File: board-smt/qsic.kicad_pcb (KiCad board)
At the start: 2 copper layers, 217.7 x 134 mm, 86 parts, among them Q201 Dual_NMOS, Q202 Dual_NMOS, Q203 Dual_NMOS, Q204 Dual_NMOS, Q205 Dual_NMOS, Q206 Dual_NMOS, Q209 Dual_NMOS, Q210 Dual_NMOS, Q211 Dual_NMOS, Q213 Dual_NMOS, Q214 Dual_NMOS, Q215 Dual_NMOS, Q218 Dual_NMOS, Q219 Dual_NMOS, Q220 Dual_NMOS, Q222 Dual_NMOS, Q223 Dual_NMOS, Q224 Dual_NMOS, Q228 Dual_NMOS, Q229 Dual_NMOS, Q232 Dual_NMOS, Q233 Dual_NMOS, Q235 Dual_NMOS, Q236 Dual_NMOS, Q239 Dual_NMOS, Q240 Dual_NMOS, Q244 Dual_NMOS, Q245 Dual_NMOS, Q247 Dual_NMOS, Q248 Dual_NMOS, Q251 Dual_NMOS, Q252 Dual_NMOS, Q254 Dual_NMOS, Q255 Dual_NMOS, Q256 Dual_NMOS, Q257 Dual_NMOS, Q258 Dual_NMOS, Q259 Dual_NMOS, Q261 Dual_NMOS

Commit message: Added board-prototype.
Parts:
- added REF**: BGA-256_pitch1mm_dia0.4mm, SMD_Packages:BGA-256_pitch1mm_dia0.4mm, F.Cu at (112.0, 72.2)
- added REF**: 10-SRT, myMods.pretty:10-SRT, F.Cu at (199.9, 48.1)
- added REF**: SOIC-16_3.9x9.9mm_Pitch1.27mm, Housings_SOIC:SOIC-16_3.9x9.9mm_Pitch1.27mm, F.Cu at (163.2, 39.2)
- moved R243 30.6 mm to (213.1, 70.1), turned to 270 degrees
- moved R245 25.3 mm to (209.2, 69.1), turned to 180 degrees
- moved R246 23.6 mm to (209.2, 76.1), turned to 180 degrees
- moved R239 21.6 mm to (213.1, 57.5), turned to 270 degrees
- moved R240 21.2 mm to (213.1, 61.0), turned to 90 degrees
- moved R241 17.7 mm to (210.8, 57.5), turned to 90 degrees
- moved R244 17.7 mm to (213.1, 73.5), turned to 90 degrees
- moved R242 16.7 mm to (210.8, 61.0), turned to 270 degrees
- moved Q256 15.5 mm to (207.3, 59.4)
- moved Q258 13.6 mm to (209.2, 72.4)
- moved R237 8.90 mm to (202.4, 72.4)
- moved R235 8.89 mm to (202.4, 59.4)
- moved R223 6.48 mm to (217.7, 62.5)
- moved R201 6.36 mm to (217.7, 65.7)
- moved R202 6.35 mm to (217.7, 78.4)
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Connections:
- B101 pad AB2: -12V -> Net-(B101-PadAB2)
- B101 pad AD2: +12V -> Net-(B101-PadAD2)
- B101 pad BB2: -12V -> Net-(B101-PadBB2)
- B101 pad BD2: +12V -> Net-(B101-PadBD2)
- Q256 pad 3: RIRQ6 -> RIAKI
- Q258 pad 3: RIRQ7 -> RDMGI
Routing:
- net (no net): track 0.00 -> 158.7 mm, vias 0 -> 12
- net +5V: track 0.00 -> 71.5 mm, vias 0 -> 4
- net GND: track 334.7 -> 372.6 mm, vias 0 -> 2
- net BDMGI: track 16.8 -> 39.5 mm
- net BDMGO: track 15.1 -> 31.5 mm
- net BIAKI: track 15.0 -> 31.1 mm
- net BIAKO: track 16.8 -> 32.6 mm
- net BBS7: track 22.5 -> 16.0 mm
- net BWTBT: track 21.8 -> 15.9 mm
- net BSYNC: track 21.8 -> 15.9 mm
- net BRPLY: track 21.8 -> 15.9 mm
- net BIRQ4: track 21.8 -> 15.9 mm
- net BINIT: track 21.8 -> 15.9 mm
- net BDOUT: track 21.8 -> 15.9 mm
- net BDIN: track 21.8 -> 15.9 mm
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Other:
- net class Default: clearance 0.254 -> 0.2032
- net class s5 added: clearance 0.127, trace_width 0.127, via_dia 0.3048, via_drill 0.254
- rule trace_clearance: 0.254 -> 0.2032

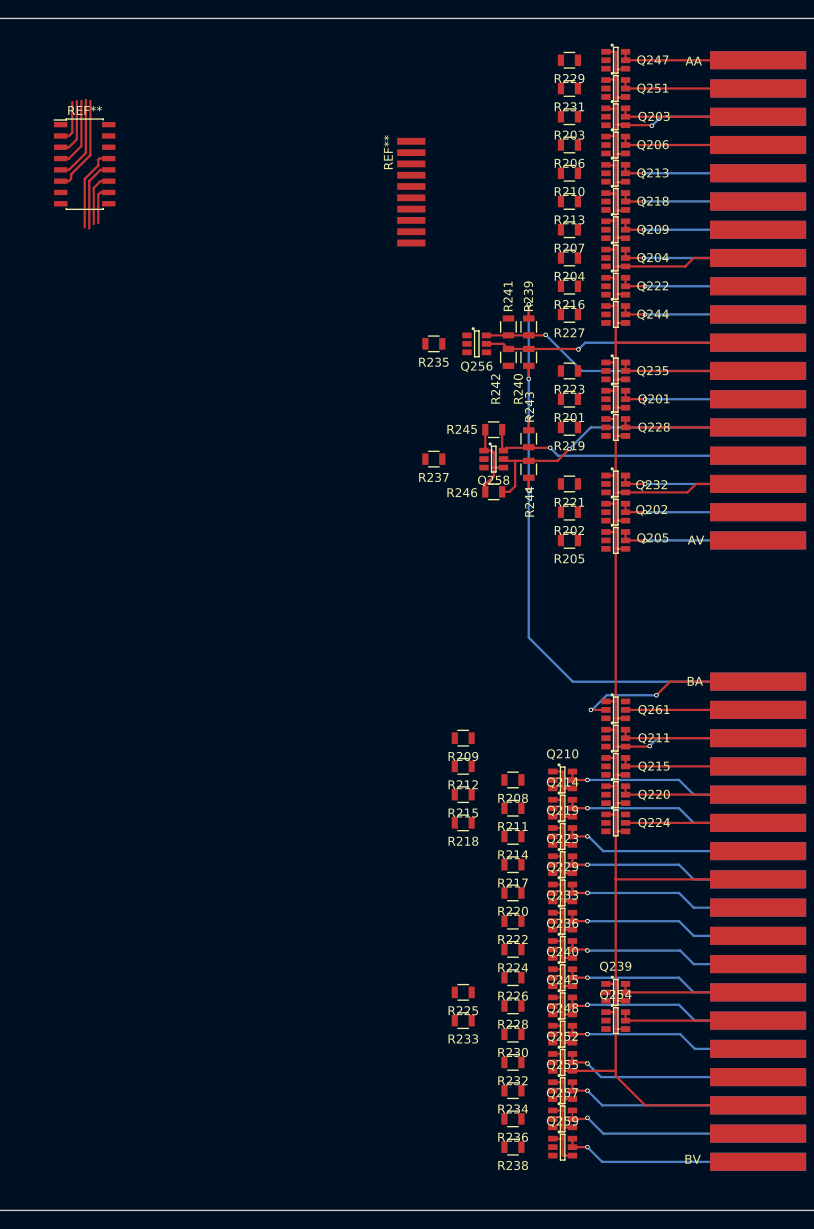
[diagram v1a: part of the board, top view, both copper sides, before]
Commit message: Added bus termination.
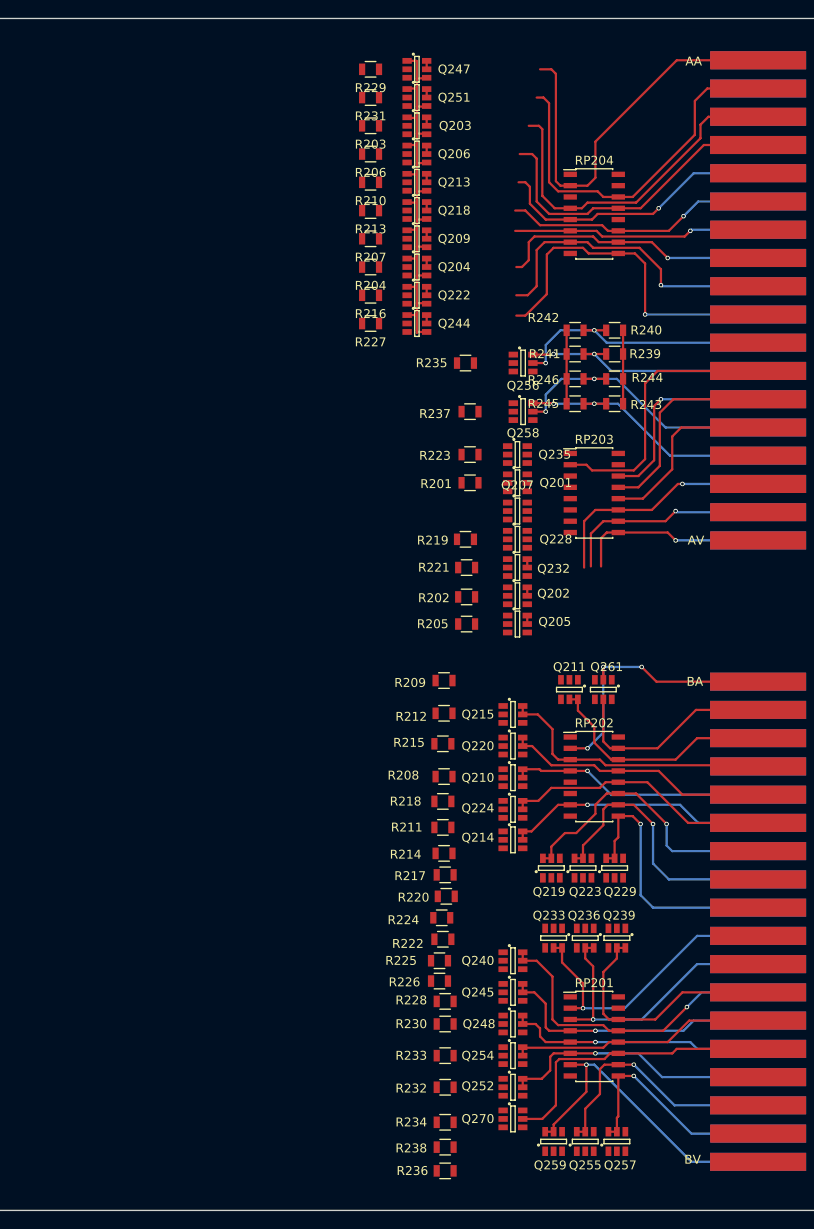
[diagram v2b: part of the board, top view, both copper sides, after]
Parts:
- removed the REF** at (199.9, 48.1)
- removed the REF** at (163.2, 39.2)
- added Q207: Dual_NMOS, TO_SOT_Packages_SMD:SOT-23-6, F.Cu at (211.8, 78.2)
- added Q270: Dual_NMOS, TO_SOT_Packages_SMD:SOT-23-6, F.Cu at (211.3, 146.6)
- added RP201: 330,680, Housings_SOIC:SOIC-16_3.9x9.9mm_Pitch1.27mm, F.Cu at (220.5, 137.3)
- added RP202: 330,680, Housings_SOIC:SOIC-16_3.9x9.9mm_Pitch1.27mm, F.Cu at (220.5, 108.1)
- added RP203: 330,680, Housings_SOIC:SOIC-16_3.9x9.9mm_Pitch1.27mm, F.Cu at (220.5, 76.2)
- added RP204: 330,680, Housings_SOIC:SOIC-16_3.9x9.9mm_Pitch1.27mm, F.Cu at (220.5, 44.8)
- B201: renamed from B101; value QBus -> QBUS
- R239, R240, R243, R244: value R -> 390
- R241, R242, R245, R246: value R -> 680
- moved Q203 22.4 mm to (200.5, 34.9)
- moved Q204 22.4 mm to (200.5, 50.8)
- moved Q206 22.4 mm to (200.5, 38.1)
- moved Q209 22.4 mm to (200.5, 47.6)
- moved Q213 22.4 mm to (200.5, 41.3)
- moved Q218 22.4 mm to (200.5, 44.5)
- moved Q222 22.4 mm to (200.5, 54.0)
- moved Q244 22.4 mm to (200.5, 57.1)
- moved Q247 22.4 mm to (200.5, 28.6)
- moved Q251 22.4 mm to (200.5, 31.8)
- moved R203 22.4 mm to (195.3, 34.9)
- moved R204 22.4 mm to (195.3, 50.8)
- moved R206 22.4 mm to (195.3, 38.1)
- moved R207 22.4 mm to (195.3, 47.6)
- moved R210 22.4 mm to (195.3, 41.3)
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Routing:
- net GND: track 372.6 -> 62.2 mm, vias 2 -> 0
- net (no net): track 158.7 -> 90.7 mm
- net +5V: track 71.5 -> 8.26 mm, vias 4 -> 0
- net BEVNT: track 0.00 -> 32.7 mm
- net BIRQ5: track 15.9 -> 46.2 mm
- net BIRQ6: track 15.9 -> 43.0 mm
- net BIRQ4: track 15.9 -> 40.3 mm
- net BDAL16: track 15.9 -> 40.1 mm
- net BHALT: track 0.00 -> 23.3 mm
- net BDAL17: track 15.9 -> 36.6 mm
- net BWTBT: track 15.9 -> 36.1 mm
- net BDOUT: track 15.9 -> 32.9 mm
- net BSYNC: track 15.9 -> 31.7 mm
- net BDAL19: track 16.0 -> 31.5 mm
- net BDAL21: track 15.0 -> 30.2 mm
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
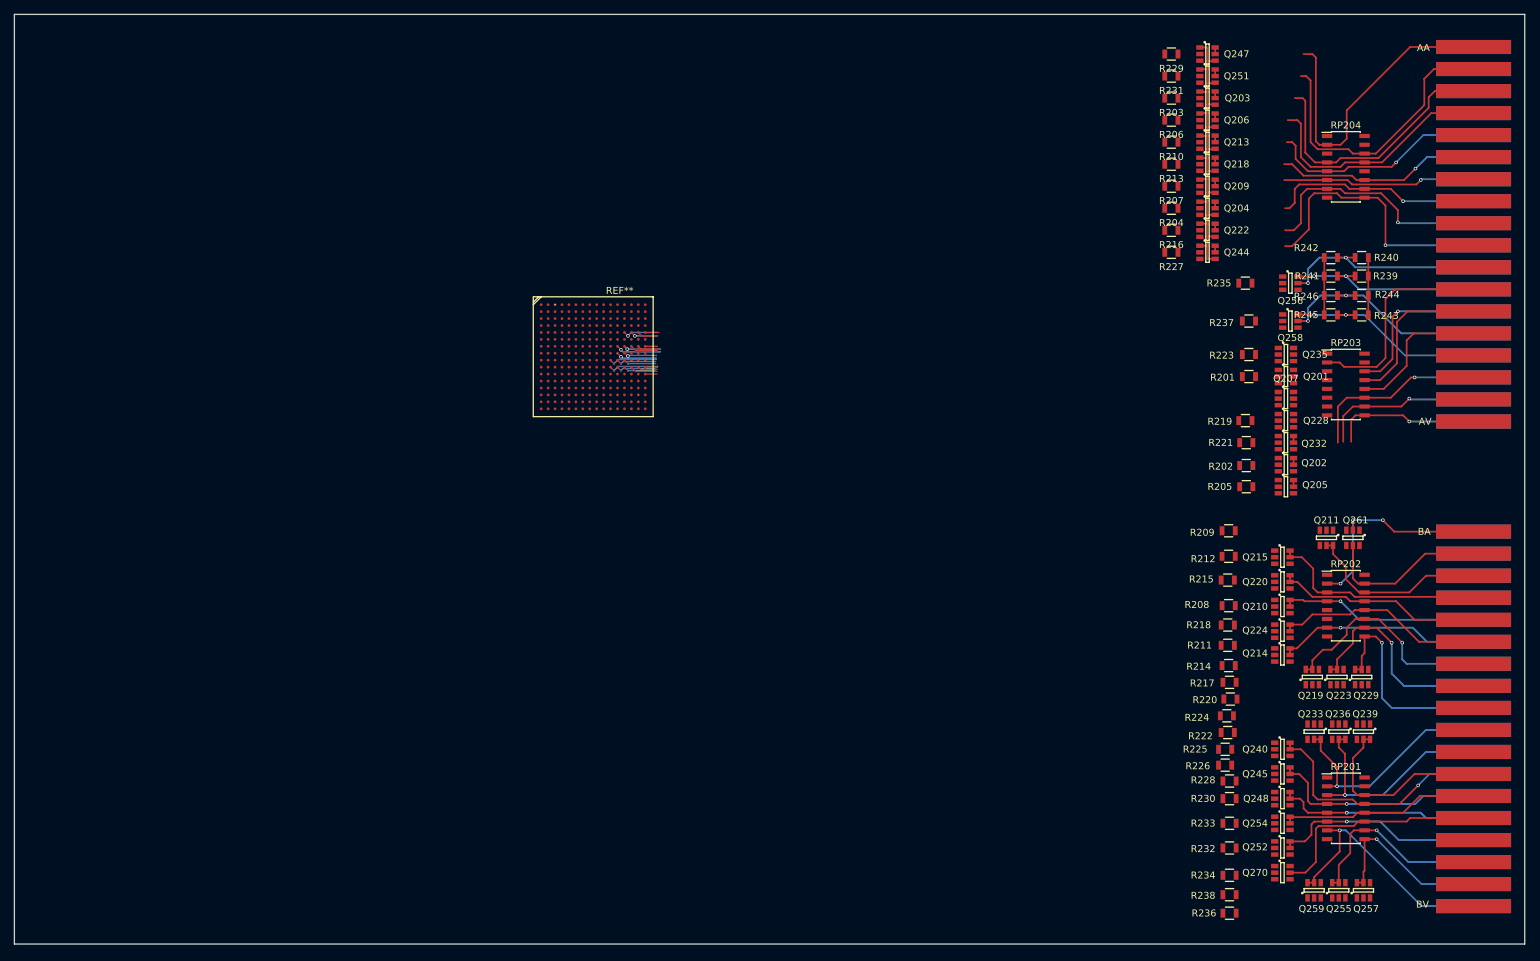
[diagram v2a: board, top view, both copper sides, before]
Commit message: Changed to comparator for bus receivers and rearranged schematic to multiple pages
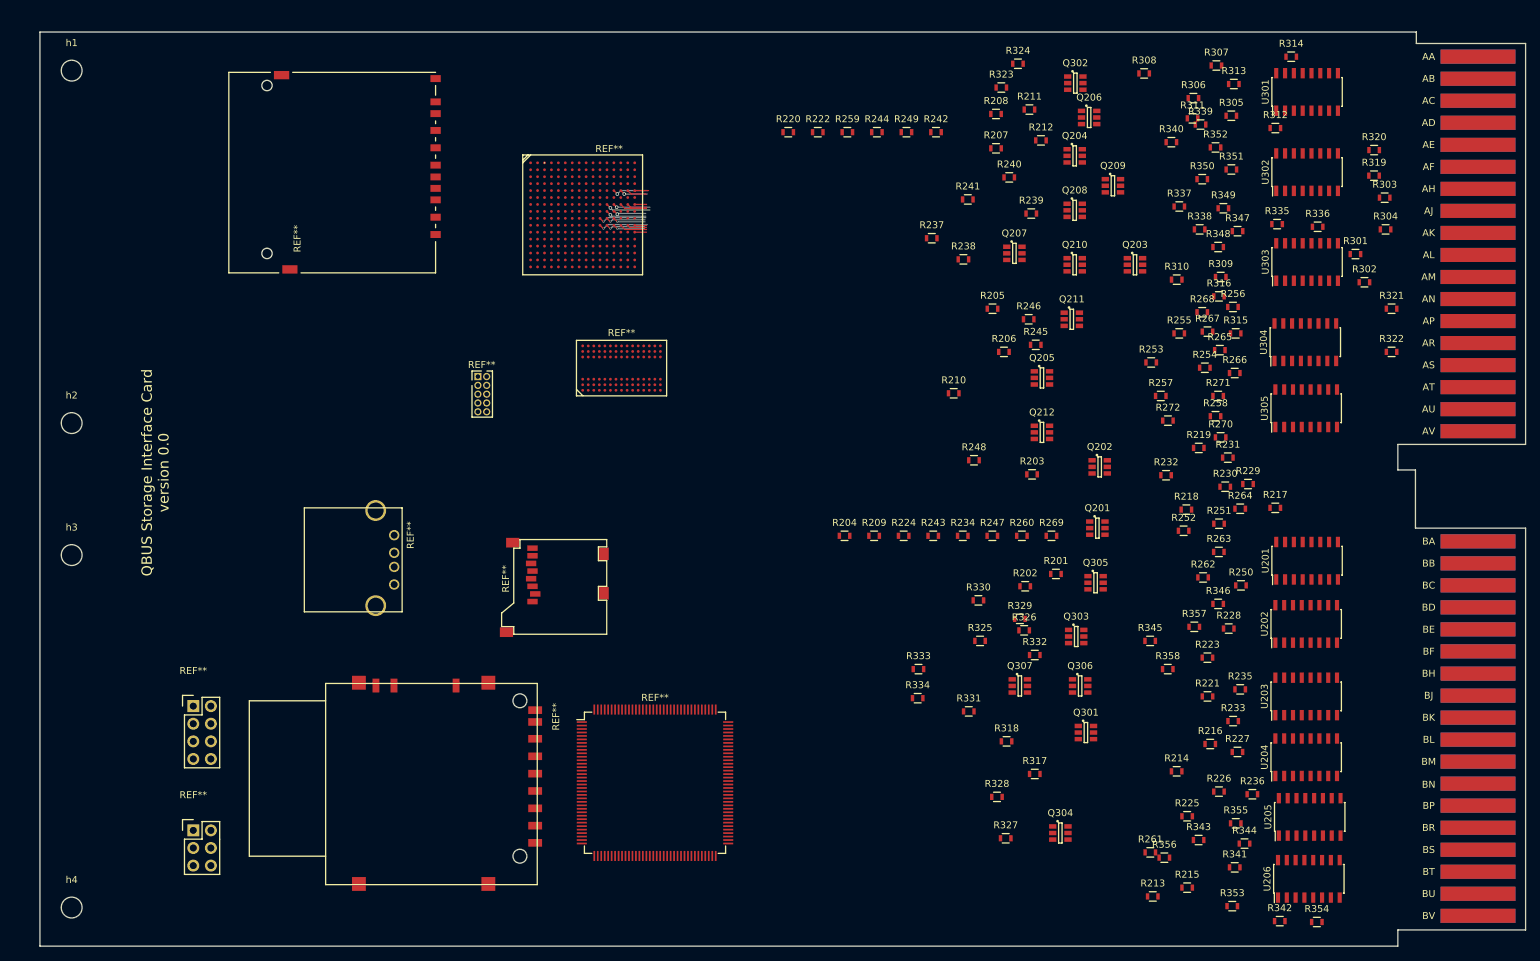
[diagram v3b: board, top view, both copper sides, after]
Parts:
- removed B201: QBUS, myMods.pretty:Qbus-double
- removed Q213, Q214, Q215, Q218, Q219, Q220, Q222, Q223, Q224, Q228, Q229, Q232, Q233, Q235, Q236, Q239, Q240, Q244, Q245, Q247, Q248, Q251, Q252, Q254, Q255, Q256, Q257, Q258, Q259, Q261, Q270: Dual_NMOS, TO_SOT_Packages_SMD:SOT-23-6
- removed RP201, RP202, RP203, RP204: 330,680, Housings_SOIC:SOIC-16_3.9x9.9mm_Pitch1.27mm
- added B101: QBUS, myMods.pretty:Qbus-double, F.Cu at (246.4, 25.4)
- added Q208: Dual_NMOS, TO_SOT_Packages_SMD:SOT-23-6, F.Cu at (181.4, 51.1)
- added Q212: Dual_NMOS, TO_SOT_Packages_SMD:SOT-23-6, F.Cu at (176.7, 83.1)
- added Q301: Dual_NMOS, TO_SOT_Packages_SMD:SOT-23-6, F.Cu at (183.0, 126.4)
- added Q302: Dual_NMOS, TO_SOT_Packages_SMD:SOT-23-6, F.Cu at (181.5, 32.8)
- added Q303: Dual_NMOS, TO_SOT_Packages_SMD:SOT-23-6, F.Cu at (181.6, 112.5)
- added Q304: Dual_NMOS, TO_SOT_Packages_SMD:SOT-23-6, F.Cu at (179.3, 140.8)
- added Q305: Dual_NMOS, TO_SOT_Packages_SMD:SOT-23-6, F.Cu at (184.4, 104.8)
- added Q306: Dual_NMOS, TO_SOT_Packages_SMD:SOT-23-6, F.Cu at (182.2, 119.6)
- added Q307: Dual_NMOS, TO_SOT_Packages_SMD:SOT-23-6, F.Cu at (173.5, 119.6)
- added R247: R, Resistors_SMD:R_0603, F.Cu at (169.5, 98.0)
- added R248: R, Resistors_SMD:R_0603, F.Cu at (166.9, 87.1)
- added R249: R, Resistors_SMD:R_0603, F.Cu at (157.1, 39.8)
- added R250: R, Resistors_SMD:R_0603, F.Cu at (205.4, 105.2)
- added R251: R, Resistors_SMD:R_0603, F.Cu at (202.2, 96.3)
- added R252: R, Resistors_SMD:R_0603, F.Cu at (197.1, 97.3)
- added R253: R, Resistors_SMD:R_0603, F.Cu at (192.4, 73.0)
- added R254: R, Resistors_SMD:R_0603, F.Cu at (200.2, 73.8)
- added R255: R, Resistors_SMD:R_0603, F.Cu at (196.5, 68.8)
- added R256: R, Resistors_SMD:R_0603, F.Cu at (204.2, 65.0)
- added R257: R, Resistors_SMD:R_0603, F.Cu at (193.8, 77.9)
- added R258: R, Resistors_SMD:R_0603, F.Cu at (201.7, 80.8)
- added R259: R, Resistors_SMD:R_0603, F.Cu at (148.6, 39.8)
- added R260: R, Resistors_SMD:R_0603, F.Cu at (173.8, 98.0)
- added R261: R, Resistors_SMD:R_0603, F.Cu at (192.3, 143.6)
- added R262: R, Resistors_SMD:R_0603, F.Cu at (199.9, 104.0)
- added R263: R, Resistors_SMD:R_0603, F.Cu at (202.2, 100.3)
- added R264: R, Resistors_SMD:R_0603, F.Cu at (205.2, 94.1)
- added R265: R, Resistors_SMD:R_0603, F.Cu at (202.3, 71.2)
- added R266: R, Resistors_SMD:R_0603, F.Cu at (204.5, 74.5)
- added R267: R, Resistors_SMD:R_0603, F.Cu at (200.5, 68.6)
- added R268: R, Resistors_SMD:R_0603, F.Cu at (199.8, 65.8)
- added R269: R, Resistors_SMD:R_0603, F.Cu at (178.0, 98.0)
- added R270: R, Resistors_SMD:R_0603, F.Cu at (202.4, 83.8)
- added R271: R, Resistors_SMD:R_0603, F.Cu at (202.1, 77.9)
- added R272: R, Resistors_SMD:R_0603, F.Cu at (194.8, 81.4)
- added R301: 330, Resistors_SMD:R_0603, F.Cu at (221.9, 57.4)
- added R302: 680, Resistors_SMD:R_0603, F.Cu at (223.2, 61.5)
- added R303: 330, Resistors_SMD:R_0603, F.Cu at (226.1, 49.3)
- added R304: 680, Resistors_SMD:R_0603, F.Cu at (226.2, 53.8)
- added R305: R, Resistors_SMD:R_0603, F.Cu at (204.0, 37.5)
- added R306: R, Resistors_SMD:R_0603, F.Cu at (198.5, 34.9)
- added R307: R, Resistors_SMD:R_0603, F.Cu at (201.8, 30.2)
- added R308: R, Resistors_SMD:R_0603, F.Cu at (191.4, 31.4)
- added R309: R, Resistors_SMD:R_0603, F.Cu at (202.4, 60.7)
- added R310: R, Resistors_SMD:R_0603, F.Cu at (196.1, 61.1)
- added R311: R, Resistors_SMD:R_0603, F.Cu at (198.4, 37.8)
- added R312: R, Resistors_SMD:R_0603, F.Cu at (210.3, 39.2)
- added R313: R, Resistors_SMD:R_0603, F.Cu at (204.3, 32.9)
- added R314: R, Resistors_SMD:R_0603, F.Cu at (212.6, 29.0)
- added R315: R, Resistors_SMD:R_0603, F.Cu at (204.6, 68.8)
- added R316: R, Resistors_SMD:R_0603, F.Cu at (202.2, 63.5)
- added R317: R, Resistors_SMD:R_0603, F.Cu at (175.6, 132.3)
- added R318: R, Resistors_SMD:R_0603, F.Cu at (171.6, 127.6)
- added R319: 330, Resistors_SMD:R_0603, F.Cu at (224.5, 46.1)
- added R320: 680, Resistors_SMD:R_0603, F.Cu at (224.5, 42.4)
- added R321: 330, Resistors_SMD:R_0603, F.Cu at (227.1, 65.3)
- added R322: 680, Resistors_SMD:R_0603, F.Cu at (227.1, 71.5)
- added R323: R, Resistors_SMD:R_0603, F.Cu at (170.8, 33.4)
- added R324: R, Resistors_SMD:R_0603, F.Cu at (173.2, 30.0)
- added R325: R, Resistors_SMD:R_0603, F.Cu at (167.8, 113.2)
- added R326: R, Resistors_SMD:R_0603, F.Cu at (174.1, 111.6)
- added R327: R, Resistors_SMD:R_0603, F.Cu at (171.4, 141.6)
- added R328: R, Resistors_SMD:R_0603, F.Cu at (170.2, 135.6)
- added R329: R, Resistors_SMD:R_0603, F.Cu at (173.5, 110.0)
- added R330: R, Resistors_SMD:R_0603, F.Cu at (167.5, 107.3)
- added R331: R, Resistors_SMD:R_0603, F.Cu at (166.1, 123.3)
- added R332: R, Resistors_SMD:R_0603, F.Cu at (175.6, 115.2)
- added R333: R, Resistors_SMD:R_0603, F.Cu at (158.9, 117.2)
- added R334: R, Resistors_SMD:R_0603, F.Cu at (158.8, 121.4)
- added R335: R, Resistors_SMD:R_0603, F.Cu at (210.6, 53.1)
- added R336: R, Resistors_SMD:R_0603, F.Cu at (216.4, 53.5)
- added R337: R, Resistors_SMD:R_0603, F.Cu at (196.5, 50.5)
- added R338: R, Resistors_SMD:R_0603, F.Cu at (199.4, 53.8)
- added R339: R, Resistors_SMD:R_0603, F.Cu at (199.5, 38.7)
- added R340: R, Resistors_SMD:R_0603, F.Cu at (195.3, 41.3)
- added R341: R, Resistors_SMD:R_0603, F.Cu at (204.5, 145.8)
- added R342: R, Resistors_SMD:R_0603, F.Cu at (210.9, 153.5)
- added R343: R, Resistors_SMD:R_0603, F.Cu at (199.3, 141.9)
- added R344: R, Resistors_SMD:R_0603, F.Cu at (205.9, 142.4)
- added R345: R, Resistors_SMD:R_0603, F.Cu at (192.3, 113.2)
- added R346: R, Resistors_SMD:R_0603, F.Cu at (202.1, 107.8)
- added R347: R, Resistors_SMD:R_0603, F.Cu at (204.9, 54.1)
- added R348: R, Resistors_SMD:R_0603, F.Cu at (202.1, 56.4)
- added R349: R, Resistors_SMD:R_0603, F.Cu at (202.8, 50.8)
- added R350: R, Resistors_SMD:R_0603, F.Cu at (199.8, 46.6)
- added R351: R, Resistors_SMD:R_0603, F.Cu at (204.0, 45.2)
- added R352: R, Resistors_SMD:R_0603, F.Cu at (201.7, 42.0)
- added R353: R, Resistors_SMD:R_0603, F.Cu at (204.1, 151.4)
- added R354: R, Resistors_SMD:R_0603, F.Cu at (216.3, 153.7)
- added R355: R, Resistors_SMD:R_0603, F.Cu at (204.6, 139.4)
- added R356: R, Resistors_SMD:R_0603, F.Cu at (194.3, 144.4)
- added R357: R, Resistors_SMD:R_0603, F.Cu at (198.6, 111.1)
- added R358: R, Resistors_SMD:R_0603, F.Cu at (194.8, 117.2)
- added REF**: microSD 3M, myMods.pretty:microSD-3M-2900-series, F.Cu at (101.3, 98.3)
- added REF**: DEC Handle, myMods.pretty:DEC-Handle, F.Cu at (32.3, 126.1)
- added REF**: DEC Handle, myMods.pretty:DEC-Handle, F.Cu at (32.3, 56.4)
- added REF**: BGA-90-0.8mm, SMD_Packages:BGA-90-0.8mm, F.Cu at (116.1, 73.8)
- added REF**: TQFP-144_20x20mm_Pitch0.5mm, Housings_QFP:TQFP-144_20x20mm_Pitch0.5mm, F.Cu at (120.9, 133.6)
- added REF**: USB_A, Connect:USB_A, F.Cu at (83.3, 97.9)
- added REF**: SD_Card_Receptacle, Connect:SD_Card_Receptacle, F.Cu at (89.3, 45.2)
- added REF**: Pin_Header_Straight_2x04, Pin_Headers:Pin_Header_Straight_2x04, F.Cu at (54.4, 122.6)
- added REF**: Pin_Header_Straight_2x03, Pin_Headers:Pin_Header_Straight_2x03, F.Cu at (54.4, 140.5)
- added REF**: Pin_Header_Straight_2x05_Pitch1.27mm, Pin_Headers:Pin_Header_Straight_2x05_Pitch1.27mm, F.Cu at (95.4, 75.1)
- added REF**: SD Card DM1, myMods.pretty:SD-Card-DM1, F.Cu at (101.4, 121.8)
- added U201: CMP401, Housings_SOIC:SOIC-16_3.9x9.9mm_Pitch1.27mm, F.Cu at (214.9, 101.6)
- added U202: CMP401, Housings_SOIC:SOIC-16_3.9x9.9mm_Pitch1.27mm, F.Cu at (214.8, 110.7)
- added U203: CMP401, Housings_SOIC:SOIC-16_3.9x9.9mm_Pitch1.27mm, F.Cu at (214.8, 121.2)
- added U204: CMP401, Housings_SOIC:SOIC-16_3.9x9.9mm_Pitch1.27mm, F.Cu at (214.8, 129.9)
- added U205: CMP401, Housings_SOIC:SOIC-16_3.9x9.9mm_Pitch1.27mm, F.Cu at (215.3, 138.5)
- added U206: CMP401, Housings_SOIC:SOIC-16_3.9x9.9mm_Pitch1.27mm, F.Cu at (215.1, 147.4)
- added U301: CMP401, Housings_SOIC:SOIC-16_3.9x9.9mm_Pitch1.27mm, F.Cu at (214.9, 34.0)
- added U302: CMP401, Housings_SOIC:SOIC-16_3.9x9.9mm_Pitch1.27mm, F.Cu at (214.9, 45.6)
- added U303: CMP401, Housings_SOIC:SOIC-16_3.9x9.9mm_Pitch1.27mm, F.Cu at (214.9, 58.5)
- added U304: CMP401, Housings_SOIC:SOIC-16_3.9x9.9mm_Pitch1.27mm, F.Cu at (214.6, 70.1)
- added U305: CMP401, Housings_SOIC:SOIC-16_3.9x9.9mm_Pitch1.27mm, F.Cu at (214.8, 79.6)
- added h1: MountingHole_3mm, Mounting_Holes:MountingHole_3mm, F.Cu at (36.8, 31.0)
- added h2: MountingHole_3mm, Mounting_Holes:MountingHole_3mm, F.Cu at (36.8, 81.8)
- added h3: MountingHole_3mm, Mounting_Holes:MountingHole_3mm, F.Cu at (36.8, 100.8)
- added h4: MountingHole_3mm, Mounting_Holes:MountingHole_3mm, F.Cu at (36.8, 151.6)
- R201, R202, R203, R204, R205, R206, R207, R208, R209, R210, R211, R212, R213, R214, R215, R216, R217, R218, R219, R220, R221, R222, R223, R224, R225, R226, R227, R228, R229, R230, R231, R232, R233, R234, R235, R236, R237, R238: footprint Resistors_SMD:R_0805 -> Resistors_SMD:R_0603
- R239, R240, R243, R244: value 390 -> R; footprint Resistors_SMD:R_0805 -> Resistors_SMD:R_0603
- R241, R242, R245, R246: value 680 -> R; footprint Resistors_SMD:R_0805 -> Resistors_SMD:R_0603
- moved R213 105.6 mm to (192.6, 150.0), turned to 0 degrees
- moved R222 104.8 mm to (144.4, 39.8), turned to 0 degrees
- moved R220 103.6 mm to (140.1, 39.8), turned to 0 degrees
- moved R238 99.3 mm to (165.4, 58.2), turned to 0 degrees
- moved R211 82.3 mm to (174.9, 36.6), turned to 0 degrees
- moved R208 78.4 mm to (170.1, 37.2), turned to 0 degrees
- moved R216 74.3 mm to (200.9, 128.0), turned to 0 degrees
- moved R244 73.7 mm to (152.9, 39.8), turned to 0 degrees
- moved R227 72.6 mm to (204.9, 129.2), turned to 0 degrees
- moved R243 69.5 mm to (161.0, 98.0), turned to 0 degrees
- moved R204 66.7 mm to (148.2, 98.0), turned to 0 degrees
- moved R212 65.8 mm to (176.5, 41.0), turned to 0 degrees
- moved R229 63.0 mm to (206.4, 90.6), turned to 0 degrees
- moved R234 62.2 mm to (165.3, 98.0), turned to 0 degrees
- moved R242 59.7 mm to (161.4, 39.8), turned to 0 degrees
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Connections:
- Q201 pad 3: RBS7 -> BDAL1
- Q201 pad 5: BBS7 -> Net-(Q201-Pad5)
- Q201 pad 6: BBS7 -> BDAL0
- Q202 pad 3: RDAL0 -> BDAL3
- Q202 pad 5: BDAL0 -> Net-(Q202-Pad5)
- Q202 pad 6: BDAL0 -> BDAL2
- Q203 pad 3: RDAL16 -> BDAL5
- Q203 pad 5: BDAL16 -> Net-(Q203-Pad5)
- Q203 pad 6: BDAL16 -> BDAL4
- Q204 pad 3: RSYNC -> BDAL7
- Q204 pad 5: BSYNC -> Net-(Q204-Pad5)
- Q204 pad 6: BSYNC -> BDAL6
- Q205 pad 3: RDAL1 -> BDAL9
- Q205 pad 5: BDAL1 -> Net-(Q205-Pad5)
- Q205 pad 6: BDAL1 -> BDAL8
- Q206 pad 3: RDAL17 -> BDAL11
- Q206 pad 5: BDAL17 -> Net-(Q206-Pad5)
- Q206 pad 6: BDAL17 -> BDAL10
- Q207 pad 1: (no net) -> GND
- Q207 pad 2: (no net) -> Net-(Q207-Pad2)
- Q207 pad 3: RHALT -> BDAL13
- Q207 pad 5: BHALT -> Net-(Q207-Pad5)
- Q207 pad 6: (no net) -> BDAL12
- Q209 pad 3: RDIN -> BDAL17
- Q209 pad 5: BDIN -> Net-(Q209-Pad5)
- Q209 pad 6: BDIN -> BDAL16
- Q210 pad 3: RDAL2 -> BDAL19
- Q210 pad 5: BDAL2 -> Net-(Q210-Pad5)
- Q210 pad 6: BDAL2 -> BDAL18
- Q211 pad 3: RDAL18 -> BDAL21
- Q211 pad 5: BDAL18 -> Net-(Q211-Pad5)
- Q211 pad 6: BDAL18 -> BDAL20
- R201 pad 2: TBS7 -> TDAL0
- R202 pad 1: Net-(Q202-Pad2) -> Net-(Q201-Pad5)
- R202 pad 2: TDAL0 -> TDAL1
- R203 pad 1: Net-(Q203-Pad2) -> Net-(Q202-Pad2)
- R203 pad 2: TDAL16 -> TDAL2
- R204 pad 1: Net-(Q204-Pad2) -> Net-(Q202-Pad5)
- R204 pad 2: TSYNC -> TDAL3
- R205 pad 1: Net-(Q205-Pad2) -> Net-(Q203-Pad2)
- R205 pad 2: TDAL1 -> TDAL4
- R206 pad 1: Net-(Q206-Pad2) -> Net-(Q203-Pad5)
- R206 pad 2: TDAL17 -> TDAL5
- R207 pad 1: Net-(Q209-Pad2) -> Net-(Q204-Pad2)
- R207 pad 2: TDIN -> TDAL6
- R208 pad 1: Net-(Q210-Pad2) -> Net-(Q204-Pad5)
- R208 pad 2: TDAL2 -> TDAL7
- R209 pad 1: Net-(Q211-Pad2) -> Net-(Q205-Pad2)
- R209 pad 2: TDAL18 -> TDAL8
- R210 pad 1: Net-(Q213-Pad2) -> Net-(Q205-Pad5)
- R210 pad 2: TDOUT -> TDAL9
- R211 pad 1: Net-(Q214-Pad2) -> Net-(Q206-Pad2)
- R211 pad 2: TDAL3 -> TDAL10
- R212 pad 1: Net-(Q215-Pad2) -> Net-(Q206-Pad5)
- R212 pad 2: TDAL19 -> TDAL11
- R213 pad 1: Net-(Q218-Pad2) -> +1V5
- R213 pad 2: TRPLY -> Net-(R213-Pad2)
- R214 pad 1: Net-(Q219-Pad2) -> +1V5
- R214 pad 2: TDAL4 -> Net-(R214-Pad2)
- R215 pad 1: Net-(Q220-Pad2) -> +1V5
- R215 pad 2: TDAL20 -> Net-(R215-Pad2)
- R216 pad 1: Net-(Q222-Pad2) -> +1V5
- R216 pad 2: TWTBT -> Net-(R216-Pad2)
- R217 pad 1: Net-(Q223-Pad2) -> +1V5
- R217 pad 2: TDAL5 -> Net-(R217-Pad2)
- R218 pad 1: Net-(Q224-Pad2) -> +1V5
- R218 pad 2: TDAL21 -> Net-(R218-Pad2)
- R219 pad 1: Net-(Q228-Pad2) -> +1V5
- R219 pad 2: TREF -> Net-(R219-Pad2)
- R220 pad 1: Net-(Q229-Pad2) -> +1V5
- R220 pad 2: TDAL6 -> Net-(R220-Pad2)
- R221 pad 1: Net-(Q232-Pad2) -> +1V5
- R221 pad 2: TINIT -> Net-(R221-Pad2)
- R222 pad 1: Net-(Q233-Pad2) -> +1V5
- R222 pad 2: TDAL7 -> Net-(R222-Pad2)
- R223 pad 1: Net-(Q235-Pad2) -> +1V5
- R223 pad 2: TDMR -> Net-(R223-Pad2)
- R224 pad 1: Net-(Q236-Pad2) -> +1V5
- R224 pad 2: TDAL8 -> Net-(R224-Pad2)
- R225 pad 1: Net-(Q239-Pad2) -> Net-(R213-Pad2)
- R225 pad 2: TSACK -> RDAL0
- R226 pad 1: Net-(Q240-Pad2) -> Net-(R214-Pad2)
- R226 pad 2: TDAL9 -> RDAL1
- R227 pad 1: Net-(Q244-Pad2) -> Net-(R215-Pad2)
- R227 pad 2: TIRQ4 -> RDAL2
- R228 pad 1: Net-(Q245-Pad2) -> Net-(R216-Pad2)
- R228 pad 2: TDAL10 -> RDAL3
- R229 pad 1: Net-(Q247-Pad2) -> Net-(R217-Pad2)
- R229 pad 2: TIRQ5 -> RDAL4
- R230 pad 1: Net-(Q248-Pad2) -> Net-(R218-Pad2)
- R230 pad 2: TDAL11 -> RDAL5
- R231 pad 1: Net-(Q251-Pad2) -> Net-(R219-Pad2)
- R231 pad 2: TIRQ6 -> RDAL6
- R232 pad 1: Net-(Q252-Pad2) -> Net-(R220-Pad2)
- R232 pad 2: TDAL12 -> RDAL7
- R233 pad 1: Net-(Q254-Pad2) -> Net-(R221-Pad2)
- R233 pad 2: TIRQ7 -> RDAL8
- R234 pad 1: Net-(Q255-Pad2) -> Net-(R222-Pad2)
- R234 pad 2: TDAL13 -> RDAL9
- R235 pad 1: Net-(Q256-Pad2) -> Net-(R223-Pad2)
- R235 pad 2: TIAKO -> RDAL10
- R236 pad 1: Net-(Q257-Pad2) -> Net-(R224-Pad2)
- R236 pad 2: TDAL14 -> RDAL11
- R237 pad 1: Net-(Q258-Pad2) -> Net-(Q207-Pad2)
- R237 pad 2: TDMGO -> TDAL12
- R238 pad 1: Net-(Q259-Pad2) -> Net-(Q207-Pad5)
- R238 pad 2: TDAL15 -> TDAL13
- R239 pad 1: +5V -> Net-(Q208-Pad2)
- R239 pad 2: BIAKO -> TDAL14
- R240 pad 1: +5V -> Net-(Q208-Pad5)
- R240 pad 2: BIAKI -> TDAL15
- R241 pad 1: BIAKO -> Net-(Q209-Pad2)
- R241 pad 2: GND -> TDAL16
- R242 pad 1: BIAKI -> Net-(Q209-Pad5)
- R242 pad 2: GND -> TDAL17
- R243 pad 1: +5V -> Net-(Q210-Pad2)
- R243 pad 2: BDMGO -> TDAL18
- R244 pad 1: +5V -> Net-(Q210-Pad5)
- R244 pad 2: BDMGI -> TDAL19
- R245 pad 1: BDMGO -> Net-(Q211-Pad2)
- R245 pad 2: GND -> TDAL20
- R246 pad 1: BDMGI -> Net-(Q211-Pad5)
- R246 pad 2: GND -> TDAL21
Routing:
- net GND: track 62.2 -> 0.00 mm
- net BIRQ5: track 46.2 -> 0.00 mm
- net BIRQ6: track 43.0 -> 0.00 mm
- net BIRQ4: track 40.3 -> 0.00 mm, vias 1 -> 0
- net BDAL16: track 40.1 -> 0.00 mm
- net BDMGI: track 37.5 -> 0.00 mm, vias 2 -> 0
- net BDAL17: track 36.6 -> 0.00 mm
- net BWTBT: track 36.1 -> 0.00 mm, vias 1 -> 0
- net BDAL15: track 35.7 -> 0.00 mm, vias 1 -> 0
- net BDAL9: track 35.3 -> 0.00 mm, vias 1 -> 0
- net BDAL7: track 33.2 -> 0.00 mm, vias 1 -> 0
- net BDAL8: track 33.1 -> 0.00 mm, vias 1 -> 0
- net BDOUT: track 32.9 -> 0.00 mm, vias 1 -> 0
- net BEVNT: track 32.7 -> 0.00 mm
- net BDAL4: track 32.7 -> 0.00 mm, vias 1 -> 0
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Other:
- board size 217.7 x 134 mm -> 214.1 x 131.7 mm
- copper layers 2 -> 4
- board text added: "QBUS Storage Interface Card version 0.0"
